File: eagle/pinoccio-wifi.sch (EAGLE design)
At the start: 17 parts, among them J1 AVR_SPI_PRG_6, U2 LDO-TPS73533

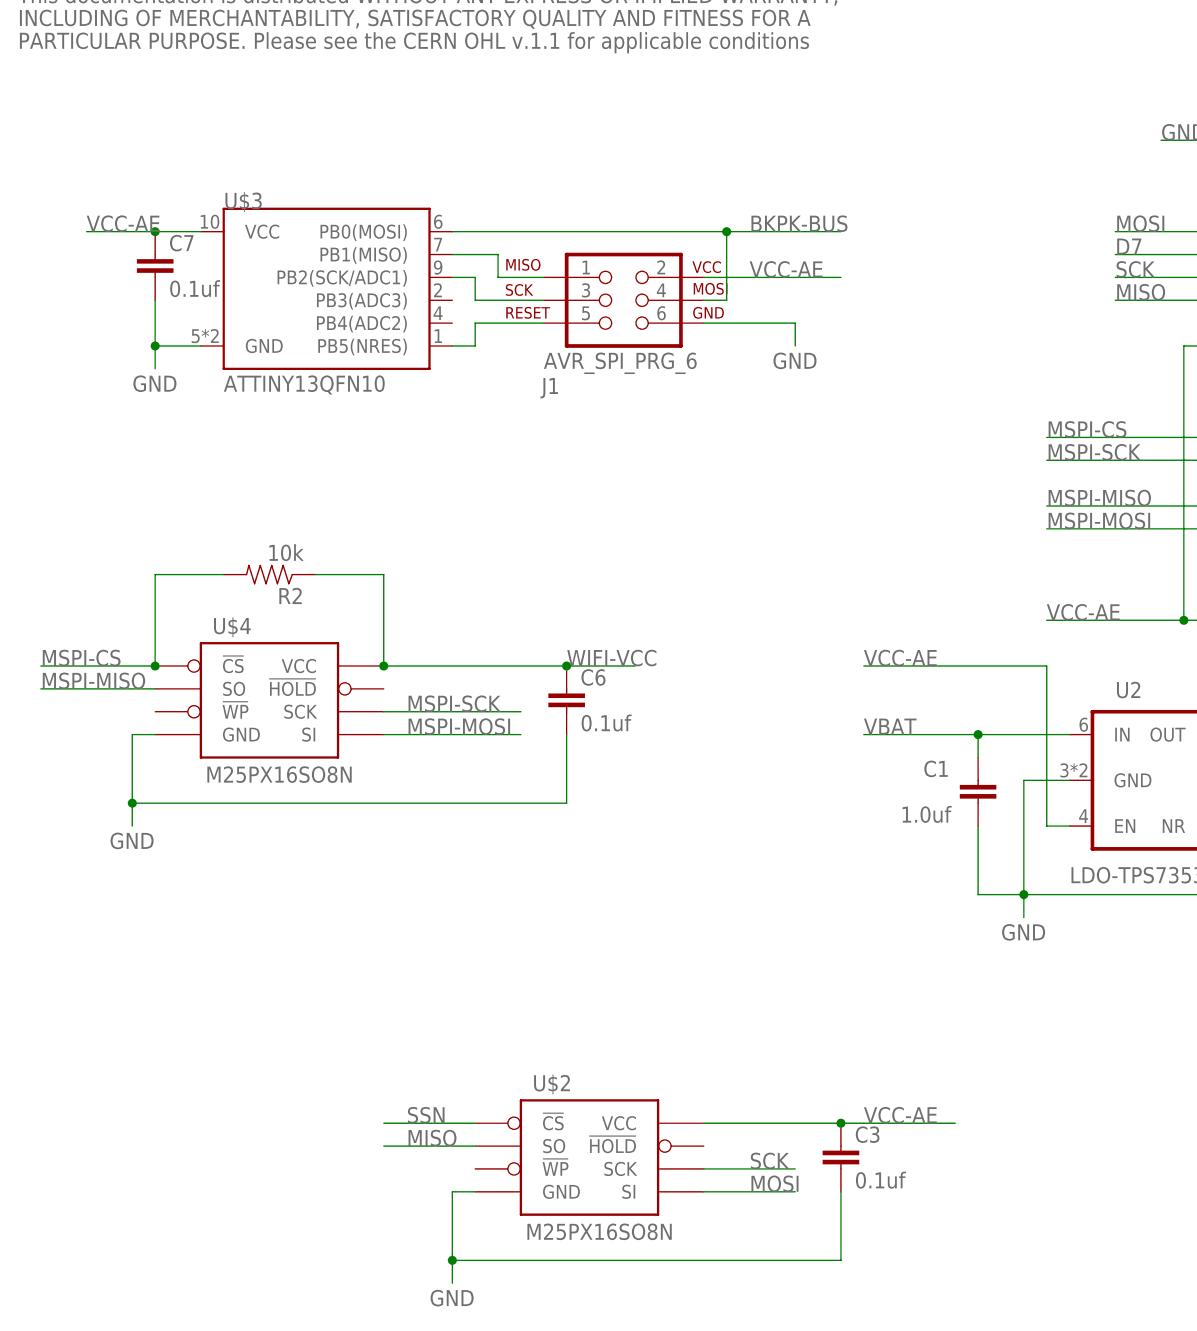
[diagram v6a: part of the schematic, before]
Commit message: update wifi to v0.13
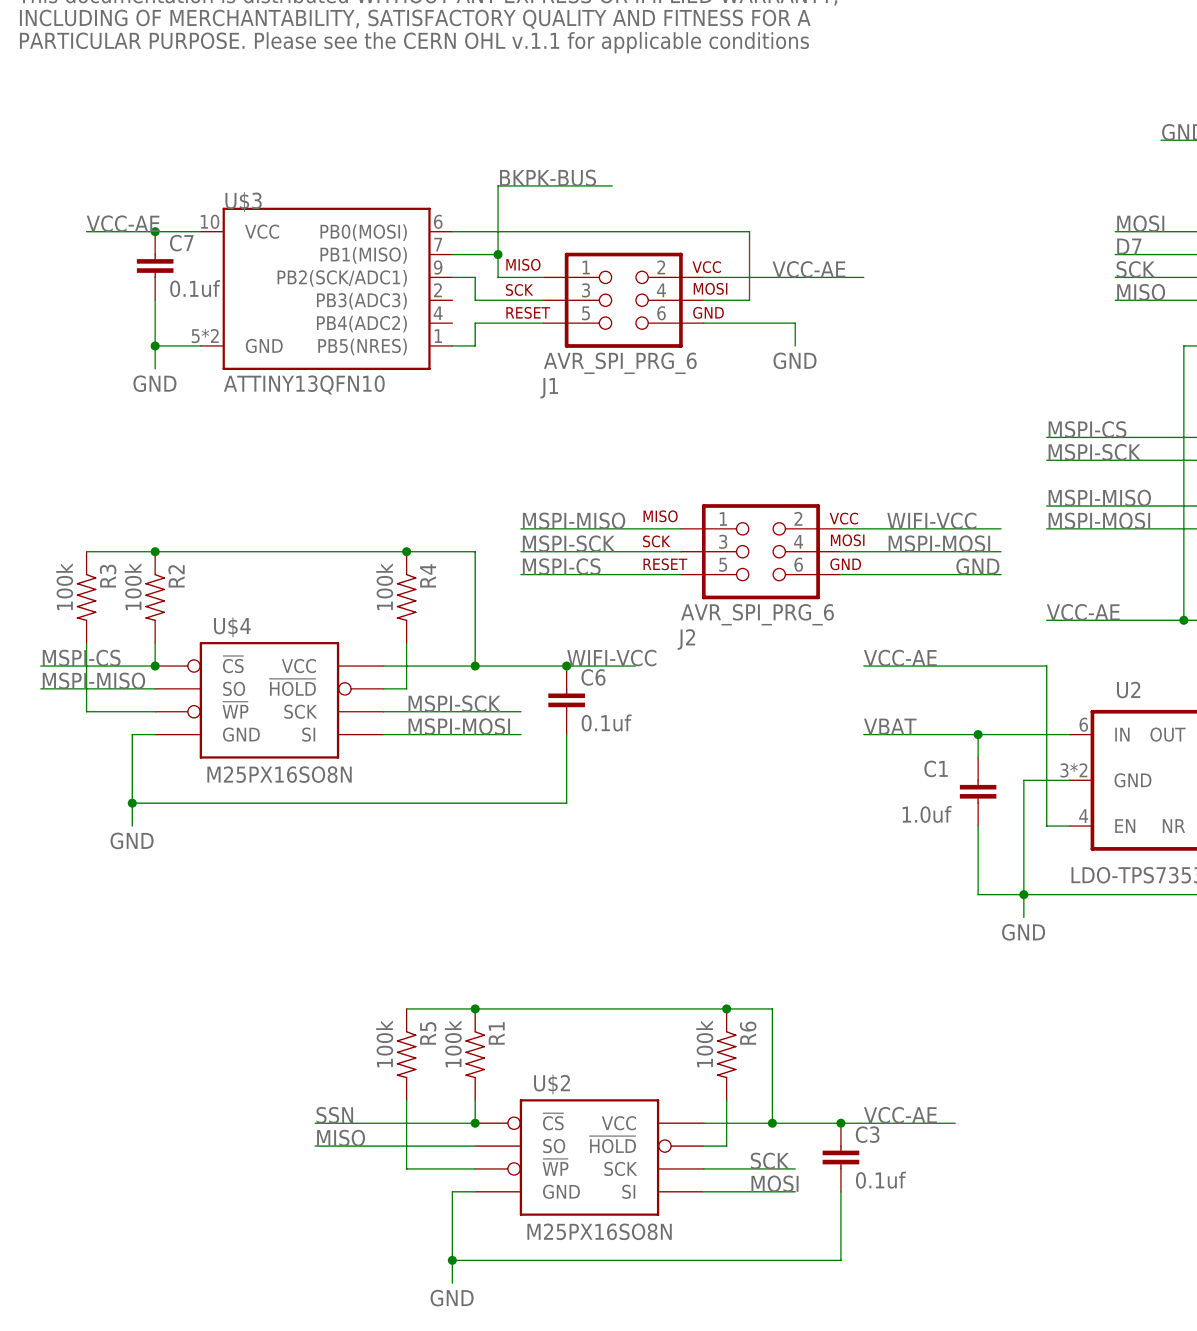
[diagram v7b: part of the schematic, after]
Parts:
- added J2: AVR_SPI_PRG_6, Pinoccio:AVR_SPI_PRG_6
- added R1, R3, R4, R5, R6: 100k, Pinoccio:RESISTOR0402-RES
- R2: value 10k -> 100k
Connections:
- new net N$1: R3.2, U$4.!WP
- new net N$5: R4.2, U$4.!HOLD
- new net N$6: R6.2, U$2.!HOLD
- new net N$7: R5.2, U$2.!WP
- net BKPK-BUS: now also J1.1, U$3.PB1(MISO); no longer J1.4, U$3.PB0(MOSI)
- net GND: now also J2.6
- net MSPI-CS: now also J2.5
- net MSPI-MISO: now also J2.1
- net MSPI-MOSI: now also J2.4
- net MSPI-SCK: now also J2.3
- net N$2: now also J1.4, U$3.PB0(MOSI); no longer J1.1, U$3.PB1(MISO)
- net SSN: now also R1.2
- net VCC-AE: now also R1.1, R5.1, R6.1
- net WIFI-VCC: now also J2.2, R3.1, R4.1
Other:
- moved on the sheet: R2

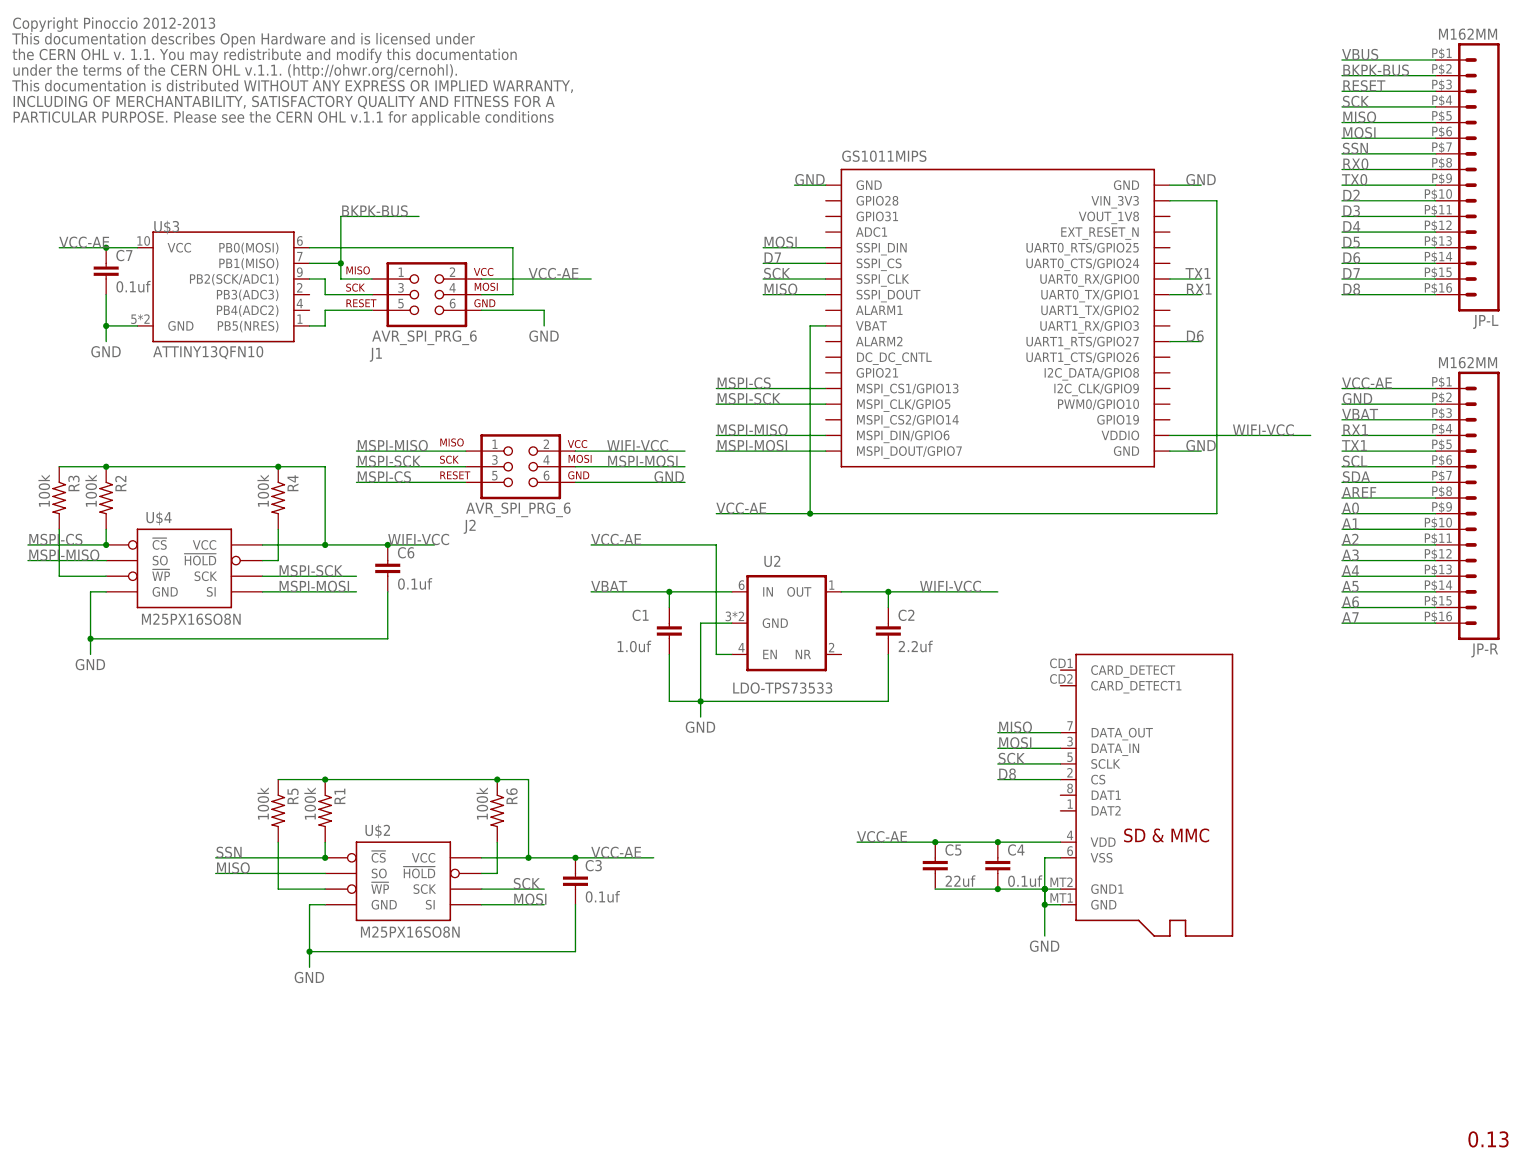
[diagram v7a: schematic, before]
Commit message: updated names of components for assembly
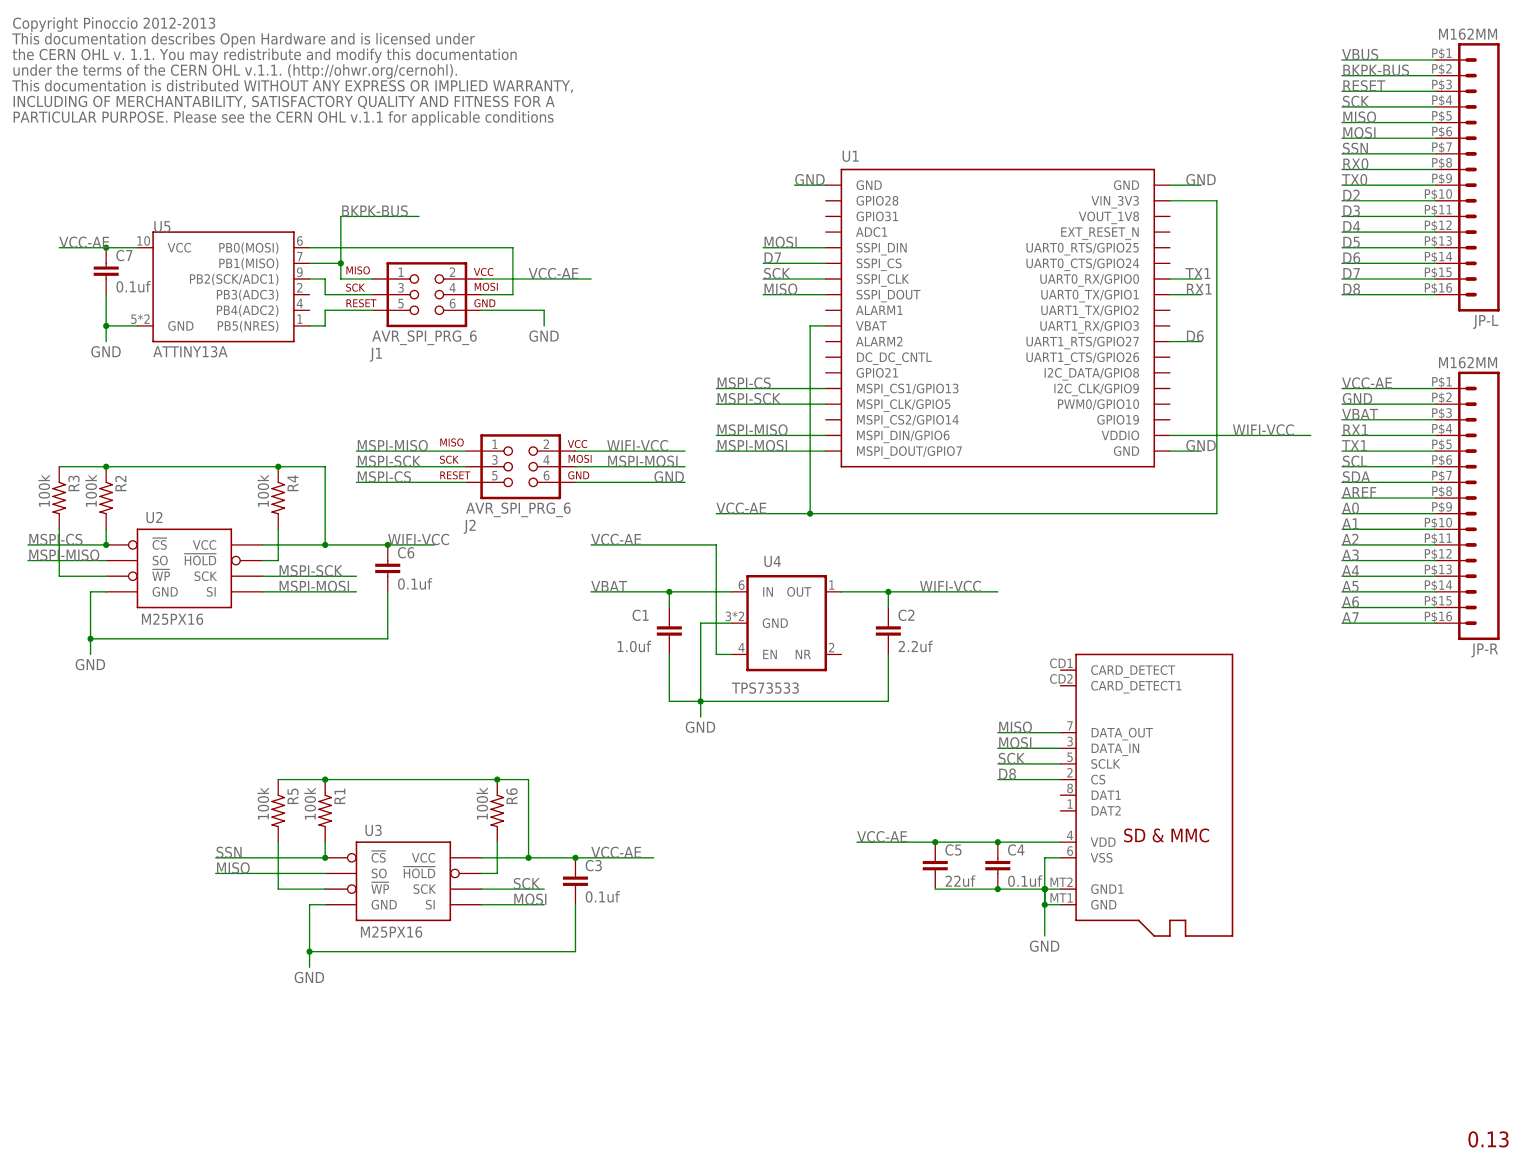
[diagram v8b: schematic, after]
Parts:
- removed U$4: M25PX16SO8N, Pinoccio:M25PX16SO8N
- added U4: TPS73533, Pinoccio:LDO-TPS73533
- U2: value LDO-TPS73533 -> M25PX16; device Pinoccio:LDO-TPS73533 -> Pinoccio:M25PX16SO8N
- U3: value M25PX16SO8N -> M25PX16
- U5: value ATTINY13QFN10 -> ATTINY13A
- renumbered GS1011MIPS to U1, U$2 to U3, U$3 to U5
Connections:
- net GND: now also U4.GND; no longer U$4.GND
- net MSPI-CS: now also U2.!CS; no longer U$4.!CS
- net MSPI-MISO: now also U2.SO; no longer U$4.SO
- net MSPI-MOSI: now also U2.SI; no longer U$4.SI
- net MSPI-SCK: now also U2.SCK; no longer U$4.SCK
- net N$1: now also U2.!WP; no longer U$4.!WP
- net N$5: now also U2.!HOLD; no longer U$4.!HOLD
- net VBAT: now also U4.IN; no longer U2.IN
- net VCC-AE: now also U4.EN; no longer U2.EN
- net WIFI-VCC: now also U2.VCC, U4.OUT; no longer U$4.VCC, U2.OUT
